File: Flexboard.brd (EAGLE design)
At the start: 488.2 x 145.3 mm, 335 parts, among them U1 MK20DN512VLQ10

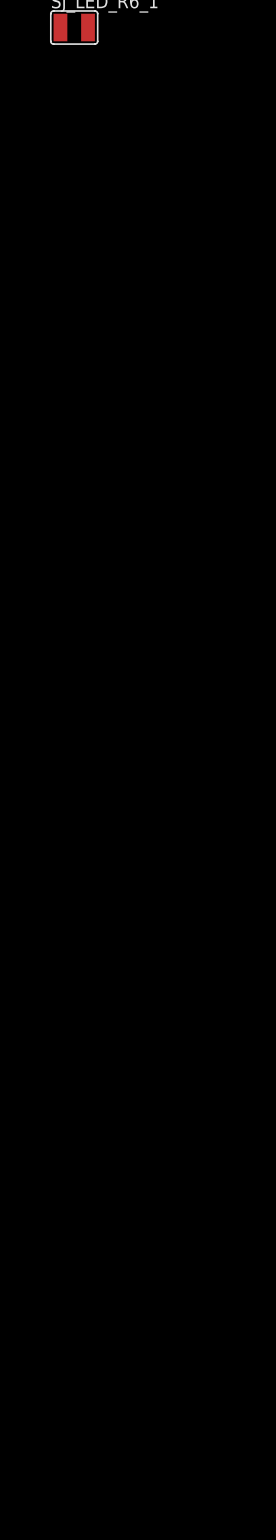
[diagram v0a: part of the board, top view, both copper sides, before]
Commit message: Routed Column Nets for LEDs
No LED traces routed on board, but all nets are routed for columns and
rows in schematic
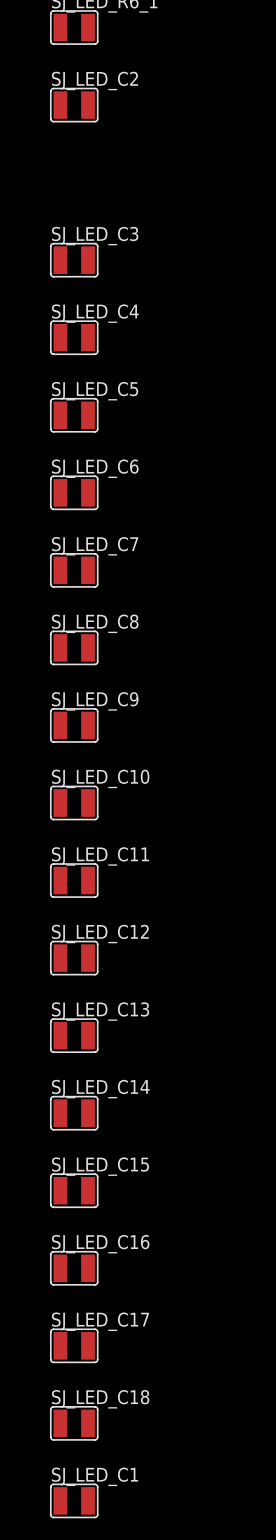
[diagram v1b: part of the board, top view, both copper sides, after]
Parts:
- added SJ_LED_C1, SJ_LED_C10, SJ_LED_C11, SJ_LED_C12, SJ_LED_C13, SJ_LED_C14, SJ_LED_C15, SJ_LED_C16, SJ_LED_C17, SJ_LED_C18, SJ_LED_C2, SJ_LED_C3, SJ_LED_C4, SJ_LED_C5, SJ_LED_C6, SJ_LED_C7, SJ_LED_C8, SJ_LED_C9: (no value), jumper:SJW
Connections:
- new net LED_COL_0: KEY_1.LED-, KEY_109.LED-, KEY_129.LED-, KEY_21.LED-, KEY_41.LED-, KEY_64.LED-, KEY_87.LED-
- new net LED_COL_1: KEY_110.LED-, KEY_130.LED-, KEY_2.LED-, KEY_22.LED-, KEY_42.LED-, KEY_65.LED-, KEY_88.LED-
- new net LED_COL_10: KEY_119.LED-, KEY_31.LED-, KEY_31_OFFSET.LED-, KEY_51.LED-, KEY_74.LED-, KEY_97.LED-, SJ_LED_C10.1
- new net LED_COL_11: KEY_120.LED-, KEY_135.LED-, KEY_32.LED-, KEY_32_OFFSET.LED-, KEY_52.LED-, KEY_75.LED-, KEY_98.LED-, SJ_LED_C11.1
- new net LED_COL_12: KEY_121.LED-, KEY_136.LED-, KEY_33.LED-, KEY_33_OFFSET.LED-, KEY_53.LED-, KEY_76.LED-, KEY_99.LED-, SJ_LED_C12.1
- new net LED_COL_13: KEY_100.LED-, KEY_137.LED-, KEY_34.LED-, KEY_54.LED-, KEY_77.LED-, SJ_LED_C13.1
- new net LED_COL_14: KEY_35.LED-, KEY_55.LED-, KEY_78.LED-, SJ_LED_C14.1
- new net LED_COL_15: KEY_36.LED-, SJ_LED_C15.1
- new net LED_COL_16: KEY_101.LED-, KEY_122.LED-, KEY_138.LED-, KEY_37.LED-, KEY_56.LED-, KEY_79.LED-, SJ_LED_C16.1
- new net LED_COL_17: KEY_102.LED-, KEY_123.LED-, KEY_139.LED-, KEY_38.LED-, KEY_57.LED-, KEY_80.LED-, SJ_LED_C17.1
- new net LED_COL_18: KEY_103.LED-, KEY_124.LED-, KEY_140.LED-, KEY_39.LED-, KEY_58.LED-, KEY_81.LED-, SJ_LED_C18.1
- new net LED_COL_19: KEY_104.LED-, KEY_125.LED-, KEY_141.LED-, KEY_40.LED-, KEY_59.LED-, KEY_82.LED-, SJ_LED_C1.1
- new net LED_COL_2: KEY_111.LED-, KEY_131.LED-, KEY_23.LED-, KEY_43.LED-, KEY_66.LED-, KEY_89.LED-, SJ_LED_C2.1
- new net LED_COL_20: KEY_105.LED-, KEY_126.LED-, KEY_142.LED-, KEY_60.LED-, KEY_83.LED-
- new net LED_COL_21: KEY_106.LED-, KEY_127.LED-, KEY_143.LED-, KEY_61.LED-, KEY_84.LED-
- new net LED_COL_22: KEY_107.LED-, KEY_128.LED-, KEY_144.LED-, KEY_62.LED-, KEY_85.LED-
- new net LED_COL_23: KEY_108.LED-, KEY_145.LED-, KEY_63.LED-, KEY_86.LED-
- new net LED_COL_3: KEY_112.LED-, KEY_132.LED-, KEY_24.LED-, KEY_44.LED-, KEY_67.LED-, KEY_90.LED-, SJ_LED_C3.1
- new net LED_COL_4: KEY_113.LED-, KEY_25.LED-, KEY_45.LED-, KEY_68.LED-, KEY_91.LED-, SJ_LED_C4.1
- new net LED_COL_5: KEY_114.LED-, SJ_LED_C5.1
- new net LED_COL_6: KEY_115.LED-, KEY_27.LED-, KEY_47.LED-, KEY_70.LED-, KEY_93.LED-, SJ_LED_C6.1
- new net LED_COL_7: KEY_116.LED-, KEY_134.LED-, KEY_28.LED-, KEY_48.LED-, KEY_71.LED-, KEY_94.LED-, SJ_LED_C7.1
- new net LED_COL_8: KEY_117.LED-, KEY_29.LED-, KEY_49.LED-, KEY_72.LED-, KEY_95.LED-, SJ_LED_C8.1
- new net LED_COL_9: KEY_118.LED-, KEY_30.LED-, KEY_30_OFFSET.LED-, KEY_50.LED-, KEY_73.LED-, KEY_96.LED-, SJ_LED_C9.1
- new net N$175: KEY_3.LED-, SJ_LED_C2.2
- new net N$186: KEY_4.LED-, SJ_LED_C3.2
- new net N$187: KEY_5.LED-, SJ_LED_C4.2
- new net N$188: KEY_6.LED-, SJ_LED_C5.2
- new net N$189: KEY_7.LED-, SJ_LED_C6.2
- new net N$190: KEY_8.LED-, SJ_LED_C7.2
- new net N$191: KEY_9.LED-, SJ_LED_C8.2
- new net N$192: KEY_10.LED-, SJ_LED_C9.2
- new net N$193: KEY_11.LED-, SJ_LED_C10.2
- new net N$194: KEY_12.LED-, SJ_LED_C11.2
- new net N$195: KEY_13.LED-, SJ_LED_C12.2
- new net N$196: KEY_14.LED-, SJ_LED_C13.2
- new net N$197: KEY_15.LED-, SJ_LED_C14.2
- new net N$198: KEY_16.LED-, SJ_LED_C15.2
- new net N$199: KEY_17.LED-, SJ_LED_C16.2
- new net N$200: KEY_18.LED-, SJ_LED_C17.2
- new net N$201: KEY_19.LED-, SJ_LED_C18.2
- new net N$202: KEY_20.LED-, SJ_LED_C1.2
- net N$1: now also KEY_69.LED-
- net N$177: now also KEY_92.LED-
- net N$2: now also KEY_26.LED-, KEY_30_OFFSET.LED+, KEY_31_OFFSET.LED+, KEY_32_OFFSET.LED+, KEY_33_OFFSET.LED+
- net N$61: now also KEY_46.LED-

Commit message: Solder joints for LEDs laid out on board
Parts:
- moved SJ_LED_C1 513.2 mm to (392.9, 123.8), flipped to the bottom, turned to 90 degrees
- moved SJ_LED_C18 494.2 mm to (373.9, 123.8), flipped to the bottom, turned to 90 degrees
- moved SJ_LED_C17 475.3 mm to (354.8, 123.8), flipped to the bottom, turned to 90 degrees
- moved SJ_LED_C16 449.6 mm to (326.2, 123.8), flipped to the bottom, turned to 90 degrees
- moved SJ_LED_C15 431.1 mm to (307.2, 123.8), flipped to the bottom, turned to 90 degrees
- moved SJ_LED_R2_1 414.9 mm to (407.4, 81.0), turned to 180 degrees
- moved SJ_LED_R3_1 414.7 mm to (408.2, 62.3), turned to 180 degrees
- moved SJ_LED_R4_1 413.4 mm to (408.2, 42.6), turned to 180 degrees
- moved SJ_LED_R6_1 412.8 mm to (408.6, 9.53), turned to 180 degrees
- moved SJ_LED_C14 412.7 mm to (288.1, 123.8), flipped to the bottom, turned to 90 degrees
- moved SJ_LED_R5_1 412.5 mm to (408.2, 23.9), turned to 180 degrees
- moved SJ_LED_C13 394.5 mm to (269.1, 123.8), flipped to the bottom, turned to 90 degrees
- moved SJ_LED_C12 376.6 mm to (250.0, 123.8), flipped to the bottom, turned to 90 degrees
- moved SJ_LED_C11 358.9 mm to (231.0, 123.8), flipped to the bottom, turned to 90 degrees
- moved SJ_LED_C10 341.5 mm to (211.9, 123.8), flipped to the bottom, turned to 90 degrees
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
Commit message: Working on moving rows to bottom layer
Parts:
- moved D20 2.38 mm to (395.3, 142.9), flipped to the bottom
- flipped D1 to the bottom
- flipped D10 to the bottom
- flipped D11 to the bottom
- flipped D12 to the bottom
- flipped D13 to the bottom
- flipped D14 to the bottom
- flipped D15 to the bottom
- flipped D16 to the bottom
- flipped D17 to the bottom
- flipped D18 to the bottom
- flipped D19 to the bottom
- flipped D2 to the bottom
- flipped D3 to the bottom
- flipped D4 to the bottom
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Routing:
- net N$35: track 10.7 -> 7.77 mm
- net N$31: track 10.7 -> 7.77 mm
- net N$29: track 10.7 -> 7.77 mm
- net N$25: track 10.7 -> 7.77 mm
- net N$15: track 10.7 -> 7.77 mm
- net N$8: track 10.7 -> 7.77 mm
- net N$23: track 10.7 -> 7.77 mm
- net N$21: track 10.7 -> 7.77 mm
- net N$19: track 10.7 -> 7.77 mm
- net N$17: track 10.7 -> 7.77 mm
- net N$13: track 10.7 -> 7.77 mm
- net N$12: track 10.7 -> 7.77 mm
- net N$6: track 10.7 -> 7.77 mm
- net N$37: track 10.7 -> 7.77 mm
- net N$33: track 10.7 -> 7.77 mm
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
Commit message: Revert "Working on moving rows to bottom layer"
This reverts commit 131a86a1cb6fe059613502008a9fd4c9c1a2df1a.
Decided it was best to leave diodes on top, so that the chip would have
more space to route in
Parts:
- moved D20 2.38 mm to (392.9, 142.9), flipped to the top
- flipped D1 to the top
- flipped D10 to the top
- flipped D11 to the top
- flipped D12 to the top
- flipped D13 to the top
- flipped D14 to the top
- flipped D15 to the top
- flipped D16 to the top
- flipped D17 to the top
- flipped D18 to the top
- flipped D19 to the top
- flipped D2 to the top
- flipped D3 to the top
- flipped D4 to the top
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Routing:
- net N$35: track 7.77 -> 10.7 mm
- net N$31: track 7.77 -> 10.7 mm
- net N$29: track 7.77 -> 10.7 mm
- net N$25: track 7.77 -> 10.7 mm
- net N$15: track 7.77 -> 10.7 mm
- net N$8: track 7.77 -> 10.7 mm
- net N$23: track 7.77 -> 10.7 mm
- net N$21: track 7.77 -> 10.7 mm
- net N$19: track 7.77 -> 10.7 mm
- net N$17: track 7.77 -> 10.7 mm
- net N$13: track 7.77 -> 10.7 mm
- net N$12: track 7.77 -> 10.7 mm
- net N$6: track 7.77 -> 10.7 mm
- net N$37: track 7.77 -> 10.7 mm
- net N$33: track 7.77 -> 10.7 mm
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
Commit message: Routed LED columns, rows partially routed
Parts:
- moved D20 2.38 mm to (395.3, 142.9)
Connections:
- net LED_COL_5: now also KEY_26.LED-, KEY_46.LED-, KEY_69.LED-, KEY_92.LED-
- net N$1: no longer KEY_69.LED-
- net N$177: no longer KEY_92.LED-
- net N$2: no longer KEY_26.LED-
- net N$61: no longer KEY_46.LED-
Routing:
- net LED_ROW_0: track 0.00 -> 399.0 mm
- net N$2: track 0.00 -> 385.3 mm, vias 0 -> 14
- net N$61: track 0.00 -> 379.9 mm, vias 0 -> 4
- net LED_COL_12: track 0.00 -> 154.6 mm
- net LED_COL_11: track 0.00 -> 153.0 mm
- net LED_COL_3: track 0.00 -> 143.9 mm
- net LED_COL_13: track 0.00 -> 139.4 mm
- net LED_COL_7: track 0.00 -> 139.0 mm
- net LED_COL_2: track 0.00 -> 135.4 mm
- net LED_COL_1: track 0.00 -> 133.8 mm
- net LED_COL_0: track 0.00 -> 133.8 mm
- net LED_COL_10: track 0.00 -> 133.0 mm
- net LED_COL_9: track 0.00 -> 132.7 mm
- net LED_COL_19: track 0.00 -> 128.5 mm
- net LED_COL_18: track 0.00 -> 128.5 mm
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
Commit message: Finished routed LEDs on PCB
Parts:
- moved U1 310.5 mm to (106.3, -64.1)
- moved D86 19.6 mm to (476.2, 76.2), turned to 270 degrees
- moved D108 19.6 mm to (476.2, 57.1), turned to 270 degrees
- moved D145 19.6 mm to (476.2, 28.6), turned to 270 degrees
- moved D63 19.6 mm to (476.2, 95.2), turned to 270 degrees
- moved D82 19.1 mm to (395.3, 76.2), turned to 270 degrees
- moved D125 19.1 mm to (395.3, 38.1), turned to 270 degrees
- moved D104 19.0 mm to (395.3, 57.1), turned to 270 degrees
- moved D59 19.0 mm to (395.3, 95.2), turned to 270 degrees
- moved D141 12.8 mm to (395.3, 19.1), turned to 270 degrees
- moved D40 8.59 mm to (400.1, 111.9)
- moved SJ_R3_1 7.83 mm to (408.6, 64.9)
- moved SJ_R5_1 7.65 mm to (408.2, 26.6)
- moved SJ_R4_1 7.59 mm to (408.6, 45.6)
- moved SJ_R2_1 7.28 mm to (408.2, 83.3)
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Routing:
- net N$1: track 0.00 -> 381.3 mm
- net N$177: track 0.00 -> 380.8 mm
- net N$181: track 0.00 -> 378.7 mm
- net N$184: track 0.00 -> 373.6 mm
- net N$185: track 0.00 -> 78.5 mm
- net N$179: track 0.00 -> 69.3 mm
- net N$173: track 0.00 -> 69.1 mm
- net N$182: track 0.00 -> 49.1 mm
- net LED_ROW_4: track 0.00 -> 37.1 mm
- net LED_ROW_3: track 0.00 -> 37.0 mm
- net LED_ROW_5: track 0.00 -> 36.1 mm
- net LED_ROW_6: track 0.00 -> 35.1 mm
- net N$151: track 72.8 -> 86.4 mm
- net N$157: track 365.2 -> 378.6 mm
- net N$71: track 15.1 -> 4.31 mm
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
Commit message: Starting designing trace routing to MCU
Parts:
- moved U1 279.4 mm to (335.9, 95.1)
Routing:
- net COL_0: track 127.1 -> 436.0 mm, vias 0 -> 1
- net LED_COL_0: track 133.8 -> 438.2 mm, vias 0 -> 1
- net COL_1: track 127.1 -> 417.7 mm, vias 0 -> 1
- net LED_COL_1: track 133.8 -> 419.8 mm, vias 0 -> 1
- net N$184: track 373.6 -> 455.8 mm, vias 0 -> 1
- net N$171: track 9.92 -> 83.6 mm, vias 0 -> 1
- net N$181: track 378.7 -> 435.3 mm, vias 0 -> 1
- net N$138: track 377.1 -> 431.7 mm, vias 0 -> 1
- net N$177: track 380.8 -> 418.9 mm, vias 0 -> 1
- net N$99: track 377.3 -> 412.7 mm, vias 0 -> 1
- net N$1: track 381.3 -> 398.9 mm, vias 0 -> 1
- net N$91: track 377.2 -> 392.4 mm, vias 0 -> 1
- net N$148: track 9.92 -> 11.3 mm, vias 0 -> 1

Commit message: Most columns are routed near the MCU
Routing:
- net COL_2: track 121.1 -> 383.2 mm, vias 0 -> 1
- net LED_COL_2: track 135.4 -> 393.0 mm, vias 0 -> 1
- net COL_3: track 130.3 -> 373.2 mm, vias 0 -> 1
- net LED_COL_3: track 143.9 -> 382.2 mm, vias 0 -> 1
- net COL_4: track 127.3 -> 350.8 mm, vias 0 -> 1
- net LED_COL_4: track 117.4 -> 336.4 mm, vias 0 -> 1
- net COL_5: track 102.4 -> 307.0 mm, vias 0 -> 1
- net LED_COL_5: track 117.4 -> 317.4 mm, vias 0 -> 1
- net COL_6: track 102.4 -> 287.7 mm, vias 0 -> 1
- net LED_COL_6: track 117.4 -> 298.1 mm, vias 0 -> 1
- net COL_7: track 122.5 -> 288.6 mm, vias 0 -> 1
- net LED_COL_7: track 139.0 -> 300.6 mm, vias 0 -> 1
- net COL_8: track 102.4 -> 249.3 mm, vias 0 -> 1
- net LED_COL_8: track 117.4 -> 259.6 mm, vias 0 -> 1
- net COL_9: track 111.1 -> 238.6 mm, vias 0 -> 1
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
